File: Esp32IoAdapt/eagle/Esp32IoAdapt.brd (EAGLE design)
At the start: 11.4 x 39.7 mm, 9 parts

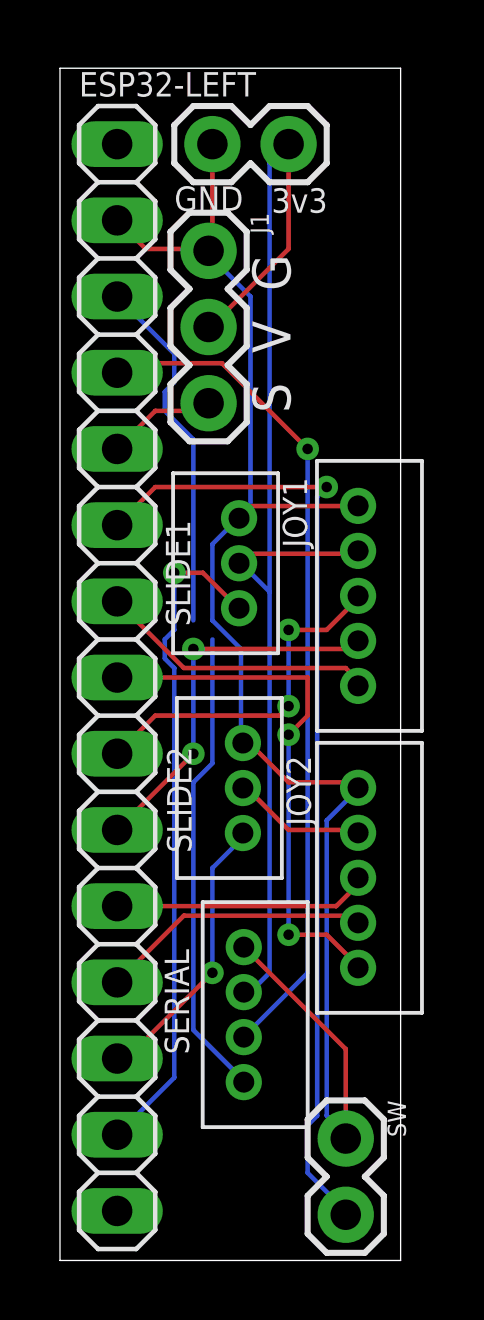
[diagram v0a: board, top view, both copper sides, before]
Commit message: Renamed connectors
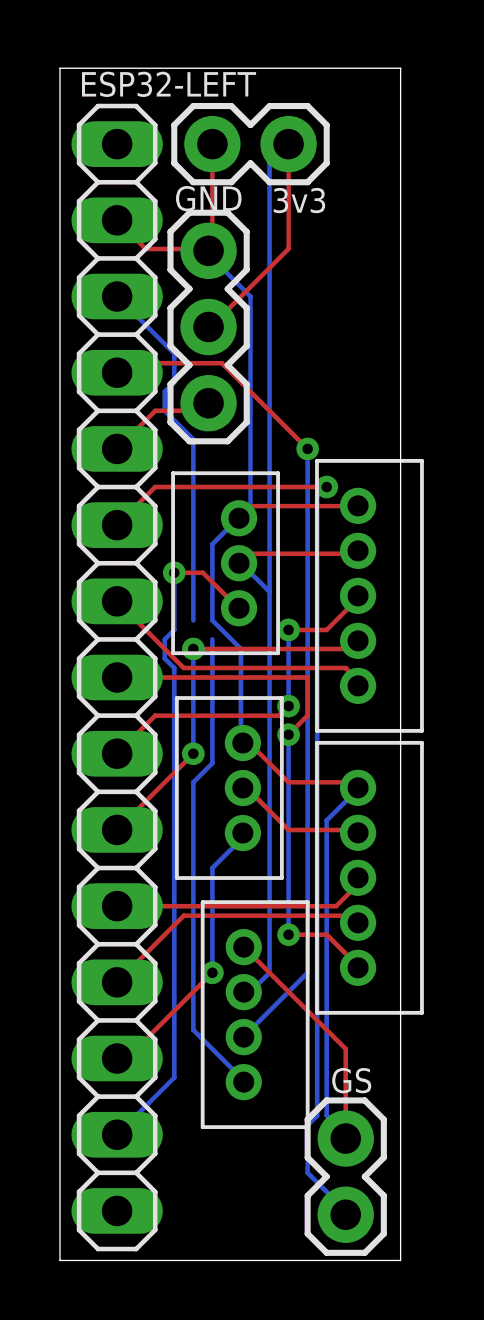
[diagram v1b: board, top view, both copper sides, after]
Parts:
- renumbered J1 to GVS, JOY1 to GVSSS, JOY2 to GVIIS, SERIAL to GVSS, SLIDE1 to GVI-1, SLIDE2 to GVI-2, SW to GS
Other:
- board text added: "GVS"
- board text added: "I/O Adapt v1.1"
- board text removed: "ESP32 I/O Adapt v1.0"
- board text removed: "S V G"

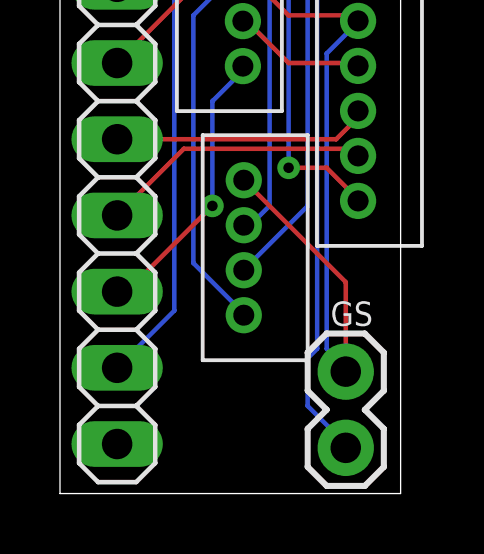
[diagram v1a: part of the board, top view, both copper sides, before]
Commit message: Adjusted labels
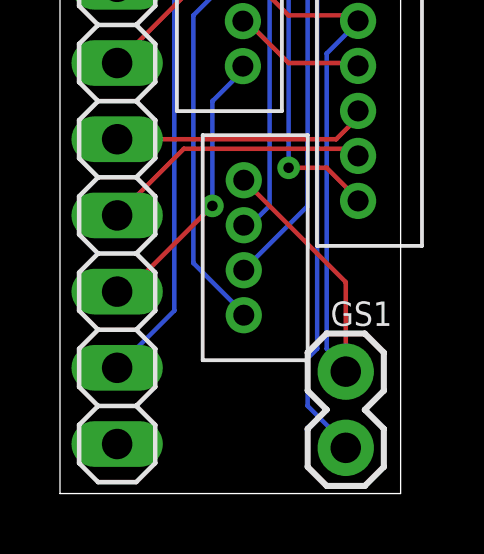
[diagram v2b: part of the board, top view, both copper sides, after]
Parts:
- renumbered GS to GS1, GVI-1 to GVI1, GVI-2 to GVI2, GVIIS to GVIIS1, GVS to GVS1, GVSS to GVSS1, GVSSS to GVSSS1
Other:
- board text added: "GVS1"
- board text removed: "GVS"
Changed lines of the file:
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@@
 <text x="4.445" y="75.2475" size="0.8128" layer="25">GND</text>
 <text x="7.6835" y="75.184" size="0.8128" layer="25">3v3</text>
-<text x="5.461" y="69.1515" size="1.27" layer="26" rot="MR90">GVS
+<text x="5.7785" y="69.1515" size="1.27" layer="26" rot="MR90">GVS1
 </text>
 <text x="11.6205" y="79.5655" size="1.27" layer="26" rot="MR270">I/O Adapt v1.1</text>
@@
 <attribute name="POPULARITY" value="4" x="2.54" y="59.69" size="1.778" layer="27" rot="R270" display="off"/>
 </element>
-<element name="GVI-1" library="jst" package="B3B-ZR" value="B3B-ZR" x="6.604" y="63.5" smashed="yes" rot="R270">
-<attribute name="NAME" x="7.8345" y="62.036" size="0.8128" layer="26" rot="MR90"/>
-</element>
-<element name="GVI-2" library="jst" package="B3B-ZR" value="B3B-ZR" x="6.731" y="56.007" smashed="yes" rot="R270">
-<attribute name="GVI-2" value="" x="7.874" y="53.848" size="0.8128" layer="26" rot="MR90" display="name"/>
-</element>
-<element name="GVSSS" library="jst" package="B5B-ZR" value="B5B-ZR" x="9.271" y="57.912" smashed="yes" rot="R90">
+<element name="GVI1" library="jst" package="B3B-ZR" value="B3B-ZR" x="6.604" y="63.5" smashed="yes" rot="R270">
+<attribute name="NAME" x="7.8345" y="62.036" size="1.27" layer="26" rot="MR90"/>
+</element>
+<element name="GVI2" library="jst" package="B3B-ZR" value="B3B-ZR" x="6.731" y="56.007" smashed="yes" rot="R270">
+<attribute name="GVI2" value="" x="7.874" y="52.2605" size="1.27" layer="26" rot="MR90" display="name"/>
+</element>
+<element name="GVSSS1" library="jst" package="B5B-ZR" value="B5B-ZR" x="9.271" y="57.912" smashed="yes" rot="R90">
 <attribute name="NAME" x="11.0965" y="60.21" size="0.8128" layer="26" rot="MR90"/>
 </element>
-<element name="GVIIS" library="jst" package="B5B-ZR" value="B5B-ZR" x="9.271" y="48.514" smashed="yes" rot="R90">
-<attribute name="NAME" x="11.2" y="51.574" size="0.8128" layer="26" rot="MR90"/>
-</element>
-<element name="GVSS" library="jst" package="B4B-ZR" value="B4B-ZR" x="5.461" y="44.704" smashed="yes" rot="R90">
-<attribute name="NAME" x="7.7945" y="47.129" size="0.8128" layer="26" rot="MR90"/>
-</element>
-<element name="GS" library="SparkFun-Connectors" library_urn="urn:adsk.eagle:library:513" package="1X02" package3d_urn="urn:adsk.eagle:package:38039/1" value="" x="10.16" y="44.323" smashed="yes" rot="R270">
+<element name="GVIIS1" library="jst" package="B5B-ZR" value="B5B-ZR" x="9.271" y="48.514" smashed="yes" rot="R90">
+<attribute name="NAME" x="11.2" y="51.2565" size="0.8128" layer="26" rot="MR90"/>
+</element>
+<element name="GVSS1" library="jst" package="B4B-ZR" value="B4B-ZR" x="5.461" y="44.704" smashed="yes" rot="R90">
+<attribute name="NAME" x="7.7945" y="43.6365" size="1.27" layer="26" rot="MR90"/>
+</element>
+<element name="GS1" library="SparkFun-Connectors" library_urn="urn:adsk.eagle:library:513" package="1X02" package3d_urn="urn:adsk.eagle:package:38039/1" value="" x="10.16" y="44.323" smashed="yes" rot="R270">
 <attribute name="NAME" x="9.652" y="45.847" size="0.8128" layer="25" font="vector" ratio="20"/>
 <attribute name="VALUE" x="8.128" y="45.593" size="0.6096" layer="27" font="vector" ratio="20" rot="R270"/>
@@
 <attribute name="VALUE" x="4.445" y="75.438" size="0.6096" layer="27" font="vector" ratio="20"/>
 </element>
-<element name="GVS" library="SparkFun-Connectors" library_urn="urn:adsk.eagle:library:513" package="1X03" package3d_urn="urn:adsk.eagle:package:38063/1" value="" x="5.588" y="73.914" smashed="yes" rot="R270">
+<element name="GVS1" library="SparkFun-Connectors" library_urn="urn:adsk.eagle:library:513" package="1X03" package3d_urn="urn:adsk.eagle:package:38063/1" value="" x="5.588" y="73.914" smashed="yes" rot="R270">
 <attribute name="VALUE" x="3.556" y="75.184" size="0.6096" layer="27" font="vector" ratio="20" rot="R270"/>
 </element>
@@
 <signal name="GND">
 <contactref element="ESP32-RIGHT" pad="2"/>
-<contactref element="GVI-1" pad="1"/>
-<contactref element="GVSSS" pad="1"/>
-<contactref element="GVI-2" pad="1"/>
-<contactref element="GVIIS" pad="1"/>
-<contactref element="GS" pad="1"/>
-<contactref element="GVSS" pad="1"/>
+<contactref element="GVI1" pad="1"/>
+<contactref element="GVSSS1" pad="1"/>
+<contactref element="GVI2" pad="1"/>
+<contactref element="GVIIS1" pad="1"/>
+<contactref element="GS1" pad="1"/>
+<contactref element="GVSS1" pad="1"/>
 <contactref element="PWR" pad="1"/>
-<contactref element="GVS" pad="1"/>
+<contactref element="GVS1" pad="1"/>
 <wire x1="10.16" y1="47.3075" x2="6.985" y2="50.4825" width="0.1524" layer="1"/>
 <wire x1="10.16" y1="44.323" x2="10.16" y2="47.3075" width="0.1524" layer="1"/>
@@
 <signal name="D13">
 <contactref element="ESP32-RIGHT" pad="3"/>
-<contactref element="GVSS" pad="4"/>
+<contactref element="GVSS1" pad="4"/>
 <wire x1="5.08" y1="47.9425" x2="6.6675" y2="46.355" width="0.1524" layer="16"/>
 <wire x1="5.08" y1="56.1975" x2="5.08" y2="47.9425" width="0.1524" layer="16"/>
@@
 <signal name="D12">
 <contactref element="ESP32-RIGHT" pad="4"/>
-<contactref element="GVSS" pad="3"/>
+<contactref element="GVSS1" pad="3"/>
 <wire x1="8.89" y1="49.8475" x2="6.985" y2="47.9425" width="0.1524" layer="16"/>
 <wire x1="8.89" y1="67.31" x2="8.89" y2="49.8475" width="0.1524" layer="16"/>
@@
 <signal name="D27">
 <contactref element="ESP32-RIGHT" pad="6"/>
-<contactref element="GS" pad="2"/>
+<contactref element="GS1" pad="2"/>
 <wire x1="3.81" y1="66.04" x2="2.54" y2="64.77" width="0.1524" layer="1"/>
 <wire x1="9.525" y1="66.04" x2="3.81" y2="66.04" width="0.1524" layer="1"/>
@@
 <signal name="D26">
 <contactref element="ESP32-RIGHT" pad="7"/>
-<contactref element="GVSSS" pad="5"/>
+<contactref element="GVSSS1" pad="5"/>
 <wire x1="10.16" y1="60.0075" x2="10.4775" y2="59.69" width="0.1524" layer="1"/>
 <wire x1="4.7625" y1="60.0075" x2="10.16" y2="60.0075" width="0.1524" layer="1"/>
@@
 <signal name="D25">
 <contactref element="ESP32-RIGHT" pad="8"/>
-<contactref element="GVIIS" pad="5"/>
+<contactref element="GVIIS1" pad="5"/>
 <wire x1="9.525" y1="51.1175" x2="10.4775" y2="50.165" width="0.1524" layer="1"/>
 <wire x1="8.255" y1="51.1175" x2="9.525" y2="51.1175" width="0.1524" layer="1"/>
@@
 <signal name="D33">
 <contactref element="ESP32-RIGHT" pad="9"/>
-<contactref element="GVSSS" pad="3"/>
+<contactref element="GVSSS1" pad="3"/>
 <wire x1="9.525" y1="61.2775" x2="10.4775" y2="62.23" width="0.1524" layer="1"/>
 <wire x1="8.255" y1="61.2775" x2="9.525" y2="61.2775" width="0.1524" layer="1"/>
@@
 <signal name="D32">
 <contactref element="ESP32-RIGHT" pad="10"/>
-<contactref element="GVSSS" pad="4"/>
+<contactref element="GVSSS1" pad="4"/>
 <wire x1="5.08" y1="60.6425" x2="10.4775" y2="60.6425" width="0.1524" layer="1"/>
 <wire x1="5.08" y1="57.15" x2="5.08" y2="60.6425" width="0.1524" layer="16"/>
@@
 <signal name="I35">
 <contactref element="ESP32-RIGHT" pad="11"/>
-<contactref element="GVIIS" pad="3"/>
+<contactref element="GVIIS1" pad="3"/>
 <wire x1="9.8425" y1="52.07" x2="10.4775" y2="52.705" width="0.1524" layer="1"/>
 <wire x1="2.54" y1="52.07" x2="9.8425" y2="52.07" width="0.1524" layer="1"/>
@@
 <signal name="I36">
 <contactref element="ESP32-RIGHT" pad="14"/>
-<contactref element="GVI-1" pad="3"/>
+<contactref element="GVI1" pad="3"/>
 <wire x1="5.3975" y1="63.1825" x2="6.35" y2="62.23" width="0.1524" layer="1"/>
 <wire x1="4.445" y1="63.1825" x2="5.3975" y2="63.1825" width="0.1524" layer="1"/>
@@
 <signal name="D14">
 <contactref element="ESP32-RIGHT" pad="5"/>
-<contactref element="GVS" pad="3"/>
+<contactref element="GVS1" pad="3"/>
 <wire x1="3.81" y1="68.58" x2="2.54" y2="67.31" width="0.1524" layer="1"/>
 <wire x1="5.3975" y1="68.58" x2="3.81" y2="68.58" width="0.1524" layer="1"/>
@@
 <signal name="I39">
 <contactref element="ESP32-RIGHT" pad="13"/>
-<contactref element="GVI-2" pad="3"/>
+<contactref element="GVI2" pad="3"/>
 <wire x1="5.715" y1="53.34" x2="6.6675" y2="54.2925" width="0.1524" layer="16"/>
 <wire x1="5.715" y1="49.8475" x2="5.715" y2="53.34" width="0.1524" layer="16"/>
@@
 <signal name="I34">
 <contactref element="ESP32-RIGHT" pad="12"/>
-<contactref element="GVIIS" pad="4"/>
+<contactref element="GVIIS1" pad="4"/>
 <wire x1="4.7625" y1="51.7525" x2="10.4775" y2="51.7525" width="0.1524" layer="1"/>
 <wire x1="2.54" y1="49.53" x2="4.7625" y2="51.7525" width="0.1524" layer="1"/>
@@
 <signal name="3V3">
 <contactref element="PWR" pad="2"/>
-<contactref element="GVSS" pad="2"/>
-<contactref element="GVIIS" pad="2"/>
-<contactref element="GVSSS" pad="2"/>
-<contactref element="GVI-2" pad="2"/>
-<contactref element="GVI-1" pad="2"/>
-<contactref element="GVS" pad="2"/>
+<contactref element="GVSS1" pad="2"/>
+<contactref element="GVIIS1" pad="2"/>
+<contactref element="GVSSS1" pad="2"/>
+<contactref element="GVI2" pad="2"/>
+<contactref element="GVI1" pad="2"/>
+<contactref element="GVS1" pad="2"/>
 <wire x1="8.255" y1="73.9775" x2="5.715" y2="71.4375" width="0.1524" layer="1"/>
 <wire x1="8.255" y1="77.47" x2="8.255" y2="73.9775" width="0.1524" layer="1"/>

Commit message: Update Esp32IoAdapt.brd
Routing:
- net D12: track 28.1 -> 39.5 mm, vias 1 -> 2
- net I34: track 9.11 -> 17.3 mm, vias 0 -> 1
- net GND: track 53.8 -> 60.2 mm
- net D26: track 9.28 -> 15.6 mm, vias 0 -> 1
- net 3V3: track 47.4 -> 42.5 mm, vias 0 -> 1
- net I36: track 22.4 -> 19.5 mm
- net D32: track 12.8 -> 10.7 mm, vias 2 -> 0
- net D33: track 11.7 -> 10.2 mm, vias 2 -> 0
- net D27: track 32.6 -> 31.3 mm
- net D25: track 18.0 -> 18.5 mm
- net D13: track 27.8 -> 28.3 mm, vias 0 -> 1

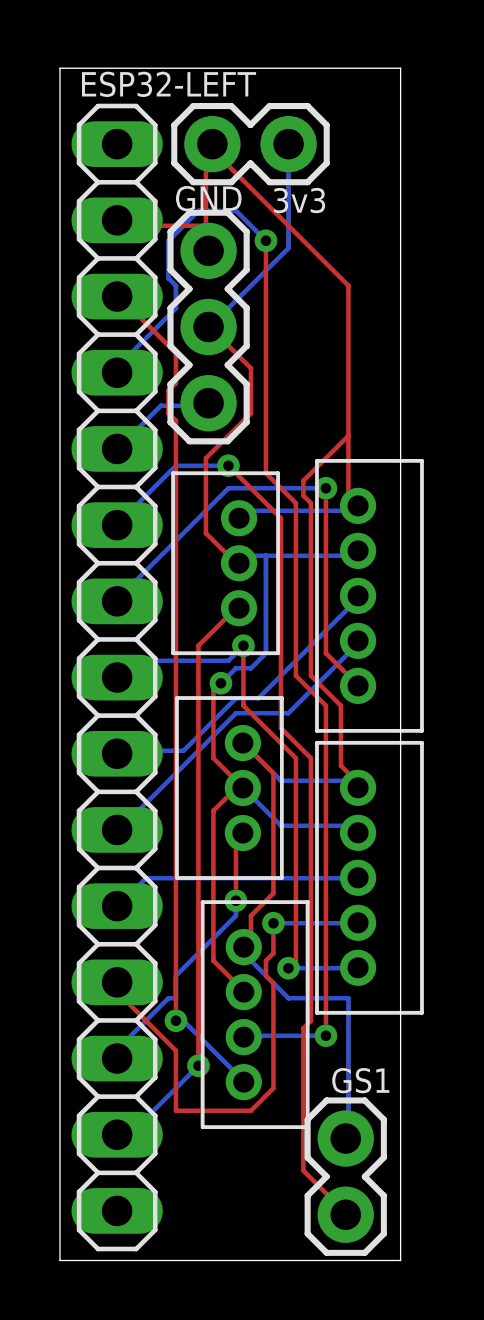
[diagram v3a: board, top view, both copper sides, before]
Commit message: More connector labelling
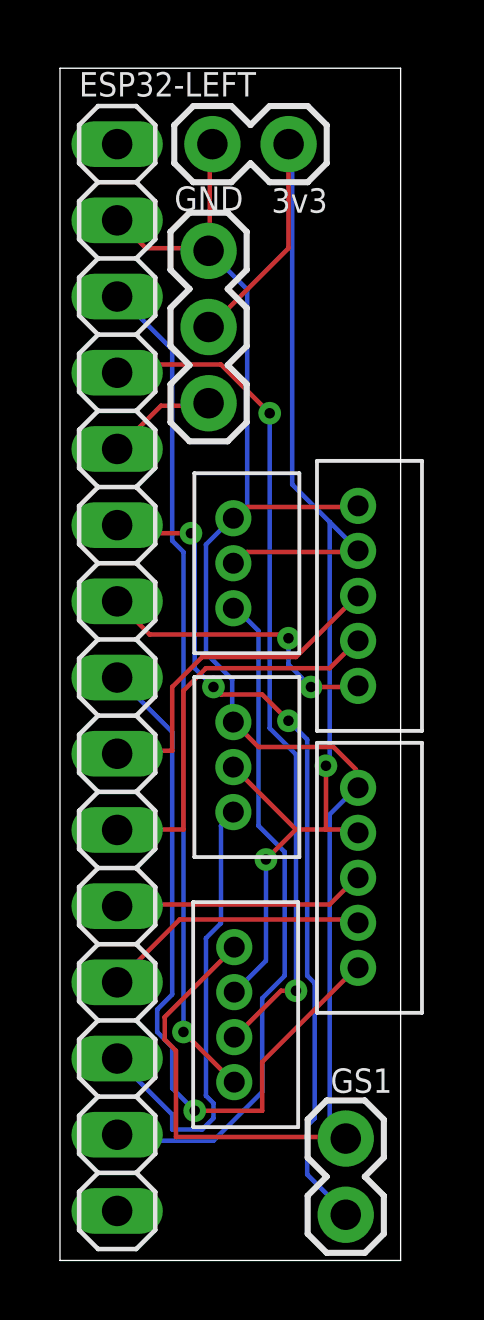
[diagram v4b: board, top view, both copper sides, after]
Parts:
- moved GVI2 0.77 mm to (6.41, 56.7), turned to 90 degrees
- moved GVSS1 0.32 mm to (5.14, 44.7)
- moved GVI1 0.19 mm to (6.41, 63.5), turned to 90 degrees
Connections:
- net GND: now also GVI1.3, GVI2.3; no longer GVI1.1, GVI2.1
- net I36: now also GVI1.1; no longer GVI1.3
- net I39: now also GVI2.1; no longer GVI2.3
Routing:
- net D12: track 39.5 -> 28.2 mm
- net I34: track 17.3 -> 8.96 mm, vias 1 -> 0
- net D26: track 15.6 -> 9.74 mm, vias 1 -> 2
- net D25: track 18.5 -> 24.3 mm, vias 2 -> 1
- net I39: track 9.64 -> 15.3 mm, vias 1 -> 0
- net 3V3: track 42.5 -> 47.7 mm, vias 1 -> 2
- net I36: track 19.5 -> 22.9 mm, vias 1 -> 0
- net D27: track 31.3 -> 28.4 mm, vias 1 -> 3
- net D32: track 10.7 -> 13.3 mm
- net D33: track 10.2 -> 11.5 mm
- net GND: track 60.2 -> 59.5 mm
